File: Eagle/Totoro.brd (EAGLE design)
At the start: 105.5 x 75.2 mm, 62 parts, among them IC1 MCP6004, J1 AUDIO_JACK_3.5MMDCI, T1 BC546A

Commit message: hw-v010
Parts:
- BAL, CUT, O1FRQ, O1FRQ1, O1FRQ2, O1FRQ3: value 100k(B) -> 10k
- OLVL: value 100k(A) -> 10k
- moved C2 5.00 mm to (79.2, 4.93)
- moved G2 5.00 mm to (40.5, 14.7)
- moved G3 5.00 mm to (61.6, 14.7)
- moved RANGE 5.00 mm to (71.6, 2.43)
- moved WAVE 5.00 mm to (97.5, 7.50)
- moved C1 5.00 mm to (67.7, 5.03)
- moved G1 5.00 mm to (19.4, 14.6)
- moved BATT1 2.00 mm to (78.0, 22.1)
- moved C7 0.46 mm to (20.8, 59.3), turned to 90 degrees
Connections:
- removed net N$30: M3.1, O1FRQ1.P$2, O1FRQ1.P$3, O1FRQ2.P$2, O1FRQ2.P$3, O1FRQ3.P$2, O1FRQ3.P$3
- net GND: now also OLVL.P$1; no longer OLVL.P$3
- net N$13: now also BAL.P$3; no longer BAL.P$1
- net N$14: now also BAL.P$1; no longer BAL.P$3
- net N$21: now also CUT.P$3; no longer CUT.P$1
- net N$22: now also OLVL.P$3; no longer OLVL.P$1
- net N$24: now also O1FRQ3.P$3; no longer O1FRQ3.P$1
- net N$26: now also O1FRQ2.P$3; no longer O1FRQ2.P$1
- net N$28: now also O1FRQ1.P$3; no longer O1FRQ1.P$1
- net N$3: now also O1FRQ.P$1; no longer O1FRQ.P$3
- net N$31: now also M3.1, O1FRQ1.P$1, O1FRQ1.P$2, O1FRQ2.P$1, O1FRQ2.P$2, O1FRQ3.P$1, O1FRQ3.P$2
- net N$8: now also O1FRQ.P$3; no longer O1FRQ.P$1
- net VSS: now also CUT.P$1; no longer CUT.P$3
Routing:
- net N$31: track 11.5 -> 90.4 mm, vias 0 -> 1
- net N$30: track 55.7 -> 0.00 mm
- net N$21: track 51.0 -> 44.4 mm
- net N$14: track 60.8 -> 67.4 mm
- net N$13: track 59.3 -> 53.3 mm
- net N$26: track 13.6 -> 19.2 mm
- net N$3: track 13.7 -> 8.34 mm
- net TRI_SAW: track 84.8 -> 89.8 mm
- net SQR: track 81.9 -> 86.9 mm
- net N$6: track 33.2 -> 38.2 mm
- net N$34: track 100.3 -> 105.3 mm
- net N$29: track 38.2 -> 43.2 mm
- net N$25: track 34.0 -> 39.0 mm
- net N$10: track 24.5 -> 29.5 mm
- net N$1: track 79.7 -> 84.7 mm
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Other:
- board size 105.5 x 75.2 mm -> 107.5 x 80.4 mm
- board text added: "+"
- board text added: "-"
- board text added: "v100"
- board text removed: "v001"

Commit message: v100 added with minor fixes and ontop batteries
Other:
- board text added: "."
- board text added: "T1"
- board text added: "designed by SyntherJack layout by snnkv.com"
- board text removed: "designed by SyntherJack re-layout by snnkv.com"

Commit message: version 101
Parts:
- renumbered O1FRQ to O2FRQ
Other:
- board text added: "v1.0.1"
- board text removed: "v100"
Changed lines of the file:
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@@
 <text x="66.8" y="-3.4" size="1.27" layer="25" font="vector" ratio="10">designed by SyntherJack
 layout by snnkv.com</text>
-<text x="94" y="-3.2" size="1.27" layer="25" font="vector" ratio="10">v100</text>
+<text x="94" y="-3.2" size="1.27" layer="25" font="vector" ratio="10">v1.0.1</text>
 <rectangle x1="87.82003125" y1="47.265671875" x2="87.87336875" y2="47.283446875" layer="200"/>
 <rectangle x1="87.80225" y1="47.28345" x2="87.87336875" y2="47.30123125" layer="200"/>
@@
 <wire x1="60.2" y1="64.5" x2="60.2" y2="59.5" width="0.1524" layer="25"/>
 <wire x1="60.2" y1="64.5" x2="60.2" y2="59.5" width="0.1524" layer="25" curve="-223.602819"/>
-<text x="49.1" y="72.3" size="1.016" layer="25">+</text>
+<text x="49.1" y="72.3" size="1.5" layer="25">+</text>
+<wire x1="88" y1="35.6" x2="89" y2="35.6" width="0.25" layer="25"/>
+<text x="18.9" y="61.3" size="1.5" layer="25">+</text>
 </plain>
 <attributes>
@@
 <elements>
 <element name="BAL" library="SparkFun-Resistors" package="POT-PTH-ALPS-KIT" value="10k" x="10.16" y="64.58" smashed="yes" rot="R270">
-<attribute name="NAME" x="10.16" y="68.168" size="1.016" layer="25" ratio="10" align="bottom-center"/>
+<attribute name="NAME" x="10.16" y="66.168" size="1.016" layer="25" ratio="10" align="bottom-center"/>
 </element>
 <element name="C1" library="rcl" library_urn="urn:adsk.eagle:library:334" package="C050-024X044" package3d_urn="urn:adsk.eagle:package:23643/1" value="10n" x="67.66" y="5.03" smashed="yes" rot="R270">
@@
 </element>
 <element name="CUT" library="SparkFun-Resistors" package="POT-PTH-ALPS-KIT" value="10k" x="73.2" y="64.45" smashed="yes" rot="R270">
-<attribute name="NAME" x="73.1" y="68.038" size="1.016" layer="25" ratio="10" align="bottom-center"/>
+<attribute name="NAME" x="73.1" y="66.038" size="1.016" layer="25" ratio="10" align="bottom-center"/>
 </element>
 <element name="D1" library="diode" library_urn="urn:adsk.eagle:library:210" package="DO35-7" package3d_urn="urn:adsk.eagle:package:43339/2" value="1N4148DO35-7" x="88.32" y="37.03" smashed="yes" rot="R90">
@@
 <attribute name="VALUE" x="93.6" y="28.686" size="0.6096" layer="27" font="vector" ratio="20" align="top-left"/>
 </element>
-<element name="O1FRQ" library="SparkFun-Resistors" package="POT-PTH-ALPS-KIT" value="10k" x="73.2" y="36.9" smashed="yes" rot="R270">
-<attribute name="NAME" x="73.2" y="40.388" size="1.016" layer="25" ratio="10" align="bottom-center"/>
+<element name="O2FRQ" library="SparkFun-Resistors" package="POT-PTH-ALPS-KIT" value="10k" x="73.2" y="36.9" smashed="yes" rot="R270">
+<attribute name="NAME" x="73.2" y="38.188" size="1.016" layer="25" ratio="10" align="bottom-center"/>
 </element>
 <element name="O1FRQ1" library="SparkFun-Resistors" package="POT-PTH-ALPS-KIT" value="10k" x="10.16" y="36.83" smashed="yes" rot="R270">
-<attribute name="NAME" x="10.16" y="40.418" size="1.016" layer="25" ratio="10" align="bottom-center"/>
+<attribute name="NAME" x="10.16" y="38.418" size="1.016" layer="25" ratio="10" align="bottom-center"/>
 </element>
 <element name="O1FRQ2" library="SparkFun-Resistors" package="POT-PTH-ALPS-KIT" value="10k" x="31.21" y="36.83" smashed="yes" rot="R270">
-<attribute name="NAME" x="31.11" y="40.218" size="1.016" layer="25" ratio="10" align="bottom-center"/>
+<attribute name="NAME" x="31.11" y="38.218" size="1.016" layer="25" ratio="10" align="bottom-center"/>
 </element>
 <element name="O1FRQ3" library="SparkFun-Resistors" package="POT-PTH-ALPS-KIT" value="10k" x="52.07" y="36.83" smashed="yes" rot="R270">
-<attribute name="NAME" x="52.07" y="40.118" size="1.016" layer="25" ratio="10" align="bottom-center"/>
+<attribute name="NAME" x="52.07" y="38.118" size="1.016" layer="25" ratio="10" align="bottom-center"/>
 </element>
 <element name="OLVL" library="SparkFun-Resistors" package="POT-PTH-ALPS-KIT" value="10k" x="31.08" y="64.58" smashed="yes" rot="R270">
-<attribute name="NAME" x="31.08" y="68.168" size="1.016" layer="25" ratio="10" align="bottom-center"/>
+<attribute name="NAME" x="31.08" y="66.168" size="1.016" layer="25" ratio="10" align="bottom-center"/>
 </element>
 <element name="R1" library="SparkFun-Resistors" package="AXIAL-0.3" value="1k" x="63.68" y="36.9" smashed="yes" rot="R270">
@@
 </element>
 <element name="WAVE" library="atarity-switch-pb22e07" package="PB22E07" value="" x="97.5" y="7.5" smashed="yes" rot="R180">
-<attribute name="NAME" x="97.98" y="5.4598" size="1.016" layer="25" ratio="10" rot="R180"/>
+<attribute name="NAME" x="97.68" y="5.4598" size="1.016" layer="25" ratio="10" rot="R180"/>
 <attribute name="POPULARITY" value="2" x="58.13" y="51.95" size="1.778" layer="27" rot="R180" display="off"/>
 <attribute name="VALUE" x="101.945" y="10.675" size="1.27" layer="27" ratio="10" rot="R180"/>
 </element>
 <element name="RANGE" library="atarity-switch-pb22e07" package="PB22E07" value="" x="71.58" y="2.43" smashed="yes">
-<attribute name="NAME" x="70.6" y="4.4702" size="1.016" layer="25" ratio="10"/>
+<attribute name="NAME" x="71.2" y="4.4702" size="1.016" layer="25" ratio="10"/>
 <attribute name="POPULARITY" value="2" x="122.38" y="-42.02" size="1.778" layer="27" display="off"/>
 <attribute name="VALUE" x="67.135" y="-0.745" size="1.27" layer="27" ratio="10"/>
 </element>
 <element name="MOD" library="atarity-switch-pb22e07" package="PB22E07" value="" x="97.53" y="39.67" smashed="yes" rot="R180">
-<attribute name="NAME" x="97.61" y="37.5298" size="1.016" layer="25" ratio="10" rot="R180"/>
+<attribute name="NAME" x="97.31" y="37.6298" size="1.016" layer="25" ratio="10" rot="R180"/>
 <attribute name="POPULARITY" value="2" x="35.3" y="84.12" size="1.778" layer="27" rot="R180" display="off"/>
 <attribute name="VALUE" x="101.975" y="42.845" size="1.27" layer="27" ratio="10" rot="R180"/>
 </element>
 <element name="RES" library="atarity-switch-pb22e07" package="PB22E07" value="" x="97.46" y="67.02" smashed="yes" rot="R180">
-<attribute name="NAME" x="97.14" y="64.8798" size="1.016" layer="25" ratio="10" rot="R180"/>
+<attribute name="NAME" x="96.94" y="64.8798" size="1.016" layer="25" ratio="10" rot="R180"/>
 <attribute name="POPULARITY" value="2" x="23.8" y="111.47" size="1.778" layer="27" rot="R180" display="off"/>
 <attribute name="VALUE" x="101.905" y="70.195" size="1.27" layer="27" ratio="10" rot="R180"/>
@@
 </element>
 <element name="POW" library="atarity-switch-pb22e07" package="PB22E07" value="" x="49.35" y="66.51" smashed="yes" rot="R270">
-<attribute name="NAME" x="51.4902" y="66.59" size="1.016" layer="25" ratio="10" rot="R270"/>
+<attribute name="NAME" x="51.4902" y="66.39" size="1.016" layer="25" ratio="10" rot="R270"/>
 <attribute name="POPULARITY" value="2" x="49.35" y="66.51" size="1.778" layer="27" rot="R270" display="off"/>
 <attribute name="VALUE" x="46.175" y="70.955" size="1.27" layer="27" ratio="10" rot="R270"/>
@@
 <signals>
 <signal name="N$2">
-<contactref element="O1FRQ" pad="P$2"/>
+<contactref element="O2FRQ" pad="P$2"/>
 <contactref element="R2" pad="P$1"/>
 <wire x1="73.2" y1="29.9" x2="73.2" y2="31.8" width="0.4064" layer="1"/>
@@
 </signal>
 <signal name="N$3">
-<contactref element="O1FRQ" pad="P$1"/>
+<contactref element="O2FRQ" pad="P$1"/>
 <contactref element="R1" pad="P$2"/>
 <wire x1="66.87" y1="29.9" x2="70.7" y2="29.9" width="0.4064" layer="1"/>
@@
 <contactref element="R6" pad="P$2"/>
 <contactref element="R5" pad="P$1"/>
-<contactref element="O1FRQ" pad="P$3"/>
+<contactref element="O2FRQ" pad="P$3"/>
 <contactref element="WAVE" pad="2"/>
 <contactref element="IC1" pad="8"/>

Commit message: 100k pot fix
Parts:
- BAL, CUT, O1FRQ1, O1FRQ2, O1FRQ3, O2FRQ: value 10k -> 100k(B)
- OLVL: value 10k -> 100k(A)
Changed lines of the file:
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@@
 </autorouter>
 <elements>
-<element name="BAL" library="SparkFun-Resistors" package="POT-PTH-ALPS-KIT" value="10k" x="10.16" y="64.58" smashed="yes" rot="R270">
+<element name="BAL" library="SparkFun-Resistors" package="POT-PTH-ALPS-KIT" value="100k(B)" x="10.16" y="64.58" smashed="yes" rot="R270">
 <attribute name="NAME" x="10.16" y="66.168" size="1.016" layer="25" ratio="10" align="bottom-center"/>
 </element>
@@
 <attribute name="PROD_ID" value="CAP-08440" x="75.38" y="75.83" size="1.778" layer="27" rot="R90" display="off"/>
 </element>
-<element name="CUT" library="SparkFun-Resistors" package="POT-PTH-ALPS-KIT" value="10k" x="73.2" y="64.45" smashed="yes" rot="R270">
+<element name="CUT" library="SparkFun-Resistors" package="POT-PTH-ALPS-KIT" value="100k(B)" x="73.2" y="64.45" smashed="yes" rot="R270">
 <attribute name="NAME" x="73.1" y="66.038" size="1.016" layer="25" ratio="10" align="bottom-center"/>
 </element>
@@
 <attribute name="VALUE" x="93.6" y="28.686" size="0.6096" layer="27" font="vector" ratio="20" align="top-left"/>
 </element>
-<element name="O2FRQ" library="SparkFun-Resistors" package="POT-PTH-ALPS-KIT" value="10k" x="73.2" y="36.9" smashed="yes" rot="R270">
+<element name="O2FRQ" library="SparkFun-Resistors" package="POT-PTH-ALPS-KIT" value="100k(B)" x="73.2" y="36.9" smashed="yes" rot="R270">
 <attribute name="NAME" x="73.2" y="38.188" size="1.016" layer="25" ratio="10" align="bottom-center"/>
 </element>
-<element name="O1FRQ1" library="SparkFun-Resistors" package="POT-PTH-ALPS-KIT" value="10k" x="10.16" y="36.83" smashed="yes" rot="R270">
+<element name="O1FRQ1" library="SparkFun-Resistors" package="POT-PTH-ALPS-KIT" value="100k(B)" x="10.16" y="36.83" smashed="yes" rot="R270">
 <attribute name="NAME" x="10.16" y="38.418" size="1.016" layer="25" ratio="10" align="bottom-center"/>
 </element>
-<element name="O1FRQ2" library="SparkFun-Resistors" package="POT-PTH-ALPS-KIT" value="10k" x="31.21" y="36.83" smashed="yes" rot="R270">
+<element name="O1FRQ2" library="SparkFun-Resistors" package="POT-PTH-ALPS-KIT" value="100k(B)" x="31.21" y="36.83" smashed="yes" rot="R270">
 <attribute name="NAME" x="31.11" y="38.218" size="1.016" layer="25" ratio="10" align="bottom-center"/>
 </element>
-<element name="O1FRQ3" library="SparkFun-Resistors" package="POT-PTH-ALPS-KIT" value="10k" x="52.07" y="36.83" smashed="yes" rot="R270">
+<element name="O1FRQ3" library="SparkFun-Resistors" package="POT-PTH-ALPS-KIT" value="100k(B)" x="52.07" y="36.83" smashed="yes" rot="R270">
 <attribute name="NAME" x="52.07" y="38.118" size="1.016" layer="25" ratio="10" align="bottom-center"/>
 </element>
-<element name="OLVL" library="SparkFun-Resistors" package="POT-PTH-ALPS-KIT" value="10k" x="31.08" y="64.58" smashed="yes" rot="R270">
+<element name="OLVL" library="SparkFun-Resistors" package="POT-PTH-ALPS-KIT" value="100k(A)" x="31.08" y="64.58" smashed="yes" rot="R270">
 <attribute name="NAME" x="31.08" y="66.168" size="1.016" layer="25" ratio="10" align="bottom-center"/>
 </element>

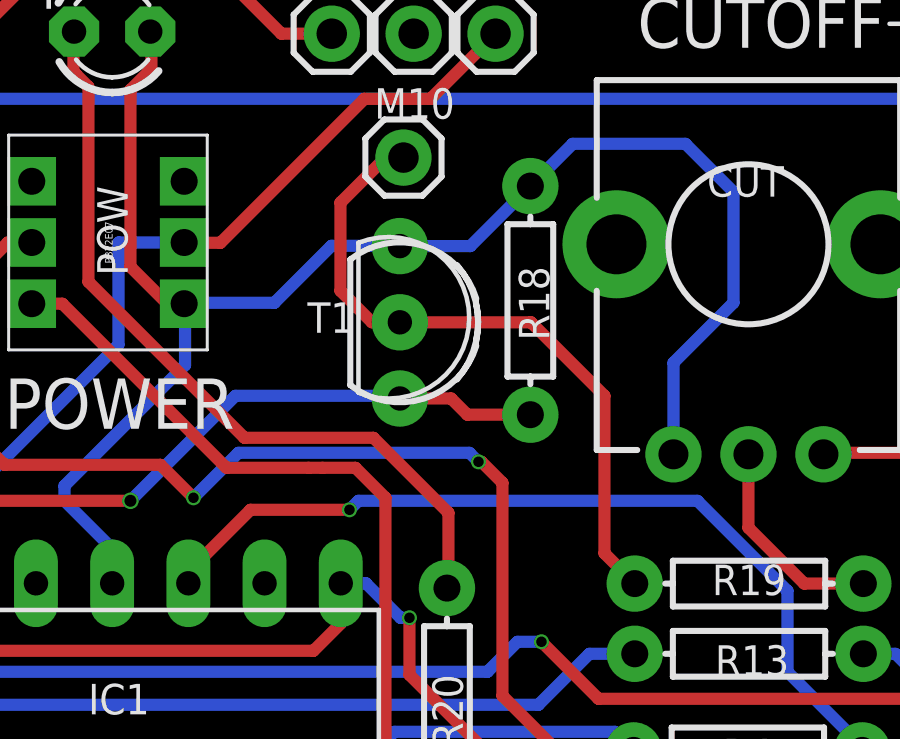
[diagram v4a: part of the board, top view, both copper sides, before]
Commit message: Transistor symbol fix
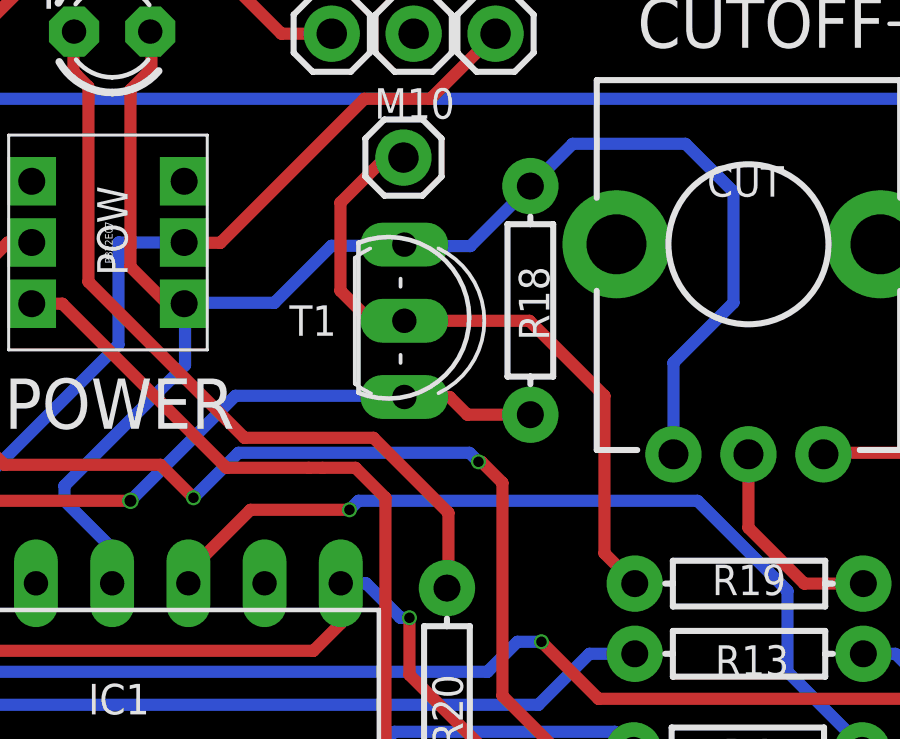
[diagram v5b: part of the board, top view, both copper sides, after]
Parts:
- T1: device User-Submitted:TO-92-AMMO -> transistor-npn:TO92-EBC
- moved T1 1.42 mm to (63.0, 61.9)
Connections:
- net N$18: now also T1.B; no longer T1.2
- net N$19: now also T1.E; no longer T1.3
- net VSS: now also T1.C; no longer T1.1
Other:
- board text removed: "T1"
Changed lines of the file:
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@@
 <text x="100.2" y="21.5" size="1.778" layer="25">-</text>
 <text x="44" y="48" size="2.54" layer="25">.</text>
-<text x="58.5" y="61.5" size="1.016" layer="25">T1</text>
 <wire x1="60.2" y1="64.5" x2="60.2" y2="59.5" width="0.1524" layer="25"/>
 <wire x1="60.2" y1="64.5" x2="60.2" y2="59.5" width="0.1524" layer="25" curve="-223.602819"/>
@@
 <attribute name="VALUE" x="101.905" y="70.195" size="1.27" layer="27" ratio="10" rot="R180"/>
 </element>
-<element name="T1" library="User-Submitted" package="TO-92-AMMO" value="BC546A" x="61.58" y="61.85" smashed="yes" rot="R270"/>
 <element name="IC1" library="linear" library_urn="urn:adsk.eagle:library:262" package="DIL14" package3d_urn="urn:adsk.eagle:package:16407/2" value="MCP6004" x="51.99" y="49.34" smashed="yes">
 <attribute name="NAME" x="51.192" y="48.781" size="1.016" layer="25" ratio="10"/>
@@
 <attribute name="NAME" x="15.83" y="31.597" size="1.016" layer="25" ratio="10"/>
 <attribute name="VALUE" x="15.33" y="28.676" size="0.6096" layer="27" font="vector" ratio="20" align="top-left"/>
+</element>
+<element name="T1" library="transistor-npn" library_urn="urn:adsk.eagle:library:398" package="TO92-EBC" package3d_urn="urn:adsk.eagle:package:28989/2" value="BC546A" x="63" y="61.9" smashed="yes" rot="R270">
+<attribute name="NAME" x="57.9" y="61.4" size="1.016" layer="25" ratio="10"/>
+<attribute name="POPULARITY" value="0" x="63" y="61.9" size="1.778" layer="27" rot="R270" display="off"/>
+<attribute name="VALUE" x="58.428" y="64.44" size="1.27" layer="27" ratio="10" rot="R270"/>
 </element>
 </elements>
@@
 <contactref element="C5" pad="2"/>
 <contactref element="R18" pad="P$2"/>
-<contactref element="T1" pad="3"/>
-<wire x1="61.58" y1="59.31" x2="63.29" y2="59.31" width="0.4064" layer="1"/>
-<wire x1="63.83" y1="58.77" x2="65.93" y2="58.77" width="0.4064" layer="1"/>
-<wire x1="63.29" y1="59.31" x2="63.83" y2="58.77" width="0.4064" layer="1"/>
+<wire x1="65.93" y1="58.77" x2="63.83" y2="58.77" width="0.4064" layer="1"/>
 <via x="52.6" y="55.9" extent="1-16" drill="0.4"/>
 <wire x1="47.42" y1="55.9" x2="52.6" y2="55.9" width="0.4064" layer="1"/>
-<wire x1="61.58" y1="59.31" x2="61.49" y2="59.4" width="0.4064" layer="16"/>
 <wire x1="61.49" y1="59.4" x2="56.1" y2="59.4" width="0.4064" layer="16"/>
 <wire x1="56.1" y1="59.4" x2="52.6" y2="55.9" width="0.4064" layer="16"/>
 <wire x1="47.42" y1="55.9" x2="44.49" y2="58.83" width="0.4064" layer="1"/>
 <wire x1="44.49" y1="58.83" x2="44.49" y2="61.91" width="0.4064" layer="1"/>
+<contactref element="T1" pad="E"/>
+<wire x1="63.24" y1="59.36" x2="61.73" y2="59.36" width="0.4064" layer="1"/>
+<wire x1="63.83" y1="58.77" x2="63.24" y2="59.36" width="0.4064" layer="1"/>
+<wire x1="61.49" y1="59.4" x2="61.73" y2="59.36" width="0" layer="19" extent="16-16"/>
 </signal>
 <signal name="VSS">
 <contactref element="R18" pad="P$1"/>
-<contactref element="T1" pad="1"/>
 <contactref element="POW" pad="6"/>
 <contactref element="LED1" pad="K"/>
 <contactref element="IC1" pad="11"/>
 <contactref element="CUT" pad="P$1"/>
-<wire x1="59.3" y1="64.4" x2="61.57" y2="64.4" width="0.4064" layer="16"/>
-<wire x1="61.57" y1="64.4" x2="61.58" y2="64.39" width="0.4064" layer="16"/>
-<wire x1="61.58" y1="64.39" x2="63.93" y2="64.39" width="0.4064" layer="16"/>
-<wire x1="63.93" y1="64.39" x2="65.93" y2="66.39" width="0.4064" layer="16"/>
+<wire x1="61.57" y1="64.4" x2="59.3" y2="64.4" width="0.4064" layer="16"/>
+<wire x1="65.93" y1="66.39" x2="63.93" y2="64.39" width="0.4064" layer="16"/>
 <wire x1="51.9" y1="54.4" x2="50.4" y2="55.9" width="0.4064" layer="16"/>
 <wire x1="51.9" y1="54.4" x2="52" y2="54.4" width="0.4064" layer="16"/>
@@
 <wire x1="70.7" y1="60.5" x2="70.7" y2="57.45" width="0.4064" layer="16"/>
 <wire x1="67.34" y1="67.8" x2="71.1" y2="67.8" width="0.4064" layer="16"/>
+<contactref element="T1" pad="C"/>
+<wire x1="63.93" y1="64.39" x2="61.78" y2="64.39" width="0.4064" layer="16"/>
+<wire x1="61.78" y1="64.39" x2="61.73" y2="64.44" width="0.1524" layer="16"/>
+<wire x1="61.57" y1="64.4" x2="61.73" y2="64.44" width="0" layer="19" extent="16-16"/>
 </signal>
 <signal name="N$16">
@@
 </signal>
 <signal name="N$18">
-<contactref element="T1" pad="2"/>
 <contactref element="R19" pad="P$1"/>
 <contactref element="M10" pad="1"/>
@@
 <wire x1="61.1" y1="67.34" x2="59.6" y2="65.84" width="0.4064" layer="1"/>
 <wire x1="59.6" y1="65.84" x2="59.6" y2="62.9" width="0.4064" layer="1"/>
-<wire x1="59.6" y1="62.9" x2="60.65" y2="61.85" width="0.4064" layer="1"/>
-<wire x1="60.65" y1="61.85" x2="61.58" y2="61.85" width="0.4064" layer="1"/>
-<wire x1="61.58" y1="61.85" x2="65.95" y2="61.85" width="0.4064" layer="1"/>
-<wire x1="65.95" y1="61.85" x2="68.4" y2="59.4" width="0.4064" layer="1"/>
+<wire x1="60.65" y1="61.85" x2="59.6" y2="62.9" width="0.4064" layer="1"/>
 <wire x1="68.4" y1="54.15" x2="69.41" y2="53.14" width="0.4064" layer="1"/>
-<wire x1="68.4" y1="59.4" x2="68.4" y2="54.15" width="0.4064" layer="1"/>
+<wire x1="68.4" y1="54.15" x2="68.4" y2="59.4" width="0.4064" layer="1"/>
+<contactref element="T1" pad="B"/>
+<wire x1="65.9" y1="61.9" x2="61.73" y2="61.9" width="0.4064" layer="1"/>
+<wire x1="68.4" y1="59.4" x2="65.9" y2="61.9" width="0.4064" layer="1"/>
+<wire x1="61.73" y1="61.9" x2="60.7" y2="61.9" width="0.4064" layer="1"/>
+<wire x1="60.7" y1="61.9" x2="60.65" y2="61.85" width="0.4064" layer="1"/>
 </signal>
 <signal name="N$21">
